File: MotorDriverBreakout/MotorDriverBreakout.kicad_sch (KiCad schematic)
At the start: 65 parts, among them U1 DRV8234RTER, U2 DRV8234RTER, U2 MCP4725A1T-E/CH, U3 MCP4725A1T-E/CH, U4 DRV8234RTER, U5 TPSM33625RDNR, U6 MCP4725A2T-E/CH, U7 TPSM33625RDNR, U8 TPSM33625RDNR, U9 INA219BIDCNT

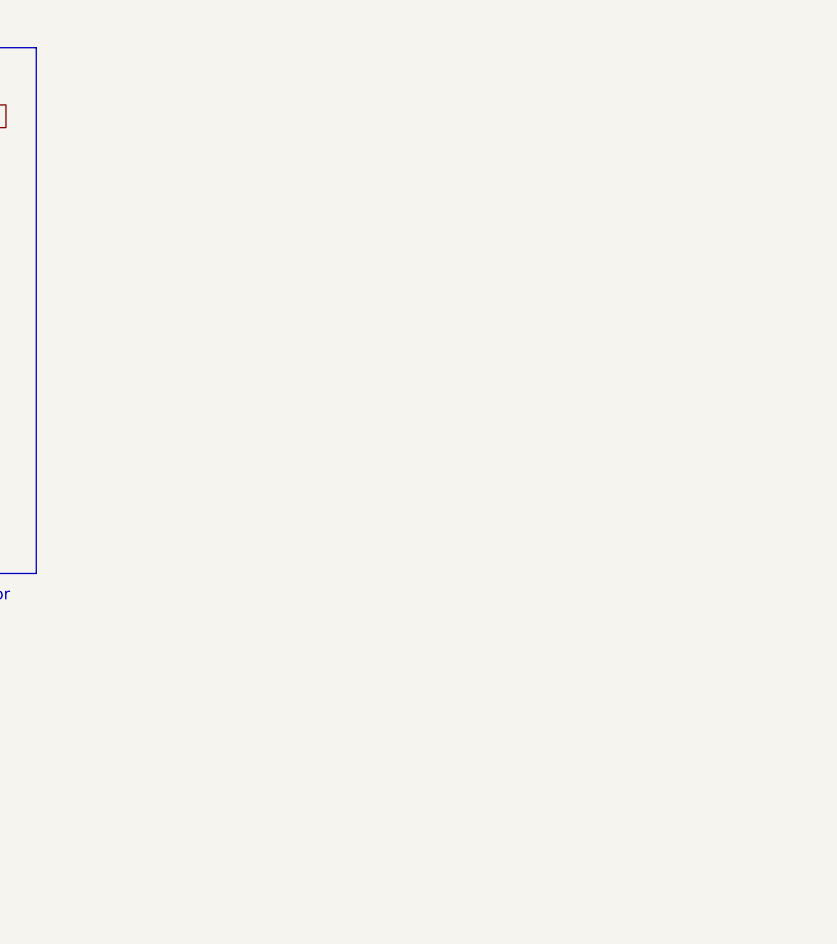
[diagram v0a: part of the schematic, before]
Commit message: Updated with connectors and through holes
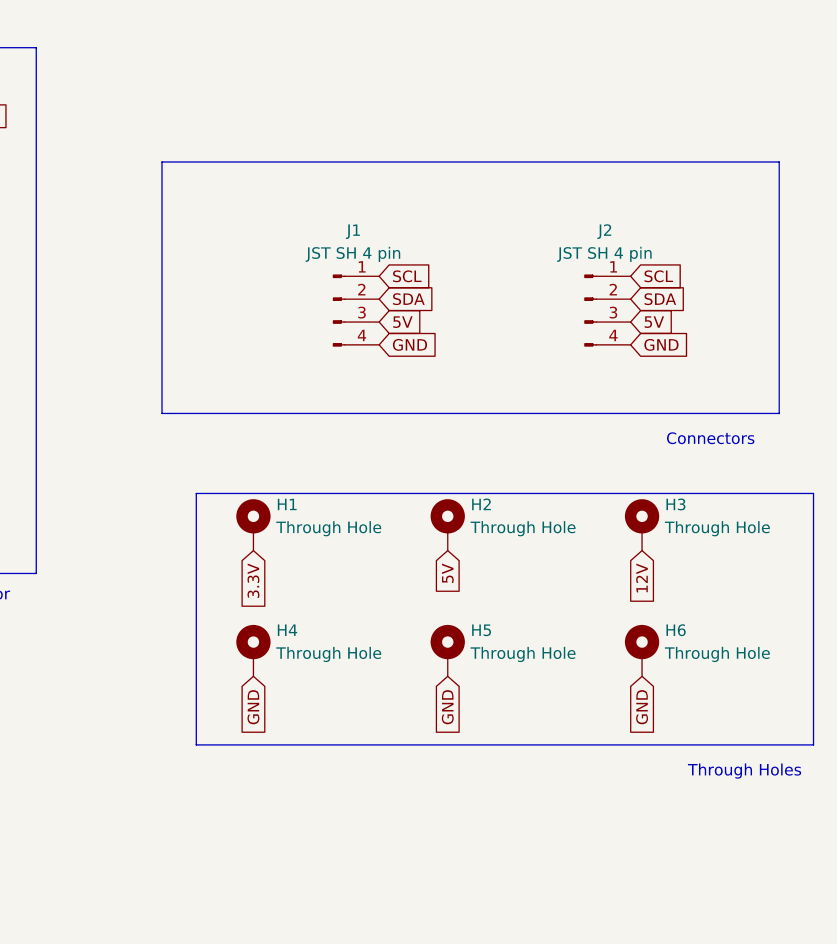
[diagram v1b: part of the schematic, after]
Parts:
- added H1, H2, H3, H4, H5, H6: Through Hole, symbol Mechanical:MountingHole_Pad
- added J1, J2: JST SH 4 pin, symbol Connector:Conn_01x04_Pin
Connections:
- net 3.3V: now also H1.1
- net GND: now also H4.1, H5.1, H6.1, J1.1 (Pin_1), J1.2 (Pin_2), J1.4 (Pin_4), J2.1 (Pin_1), J2.2 (Pin_2), J2.4 (Pin_4)
- new net 12V: H3.1
- new net 5V: H2.1, J1.3 (Pin_3), J2.3 (Pin_3)
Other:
- note added: "Connectors"
- note added: "Through Holes"

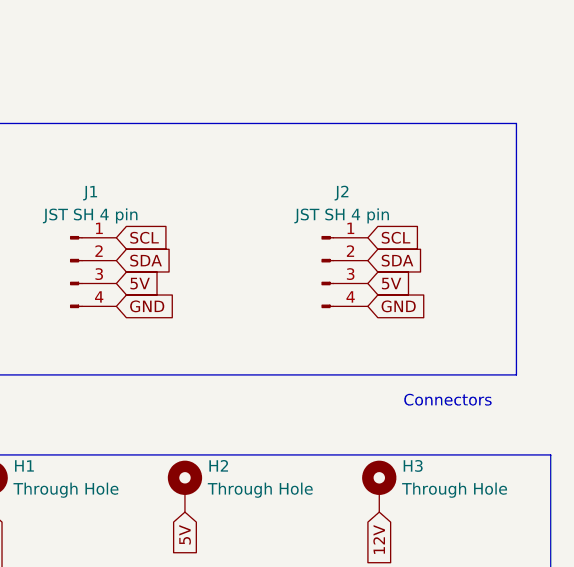
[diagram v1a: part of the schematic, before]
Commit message: Minor JST voltage Modification
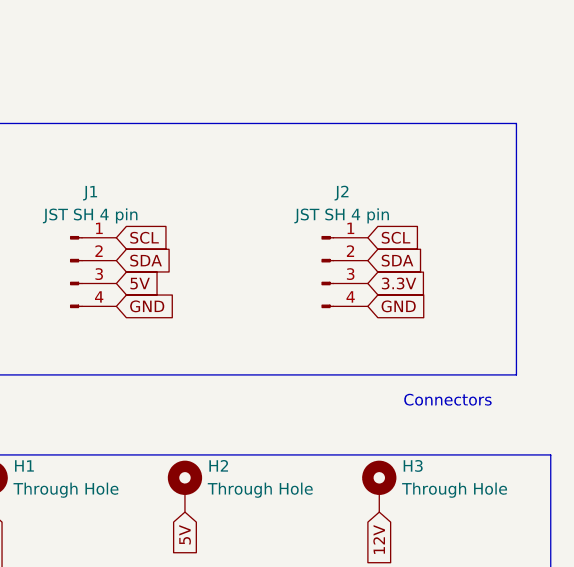
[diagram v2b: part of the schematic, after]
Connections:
- net 3.3V: now also J2.3 (Pin_3)
- net 5V: no longer J2.3 (Pin_3)
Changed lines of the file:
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@@
 		)
 	)
-	(global_label "5V"
+	(global_label "3.3V"
 		(shape input)
 		(at 553.72 205.74 0)
@@
 		)
 		(property "Intersheetrefs" "${INTERSHEET_REFS}"
-			(at 559.0033 205.74 0)
+			(at 560.8176 205.74 0)
 			(effects
 				(font
